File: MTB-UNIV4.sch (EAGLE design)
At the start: 122 parts, among them IC1 MEGA128-A, IC2 SN75176BP, IC3 MC7805CDTG, IC4 ULN2803A, IC5 ULN2803A, Q1 14.7456 MHz, X1A MVE252-5-V, X1B MVE252-5-V, X2A MVE252-5-V, X2B MVE252-5-V, X3 1751316, X4 1751316, X5 1751316, X6 1751316

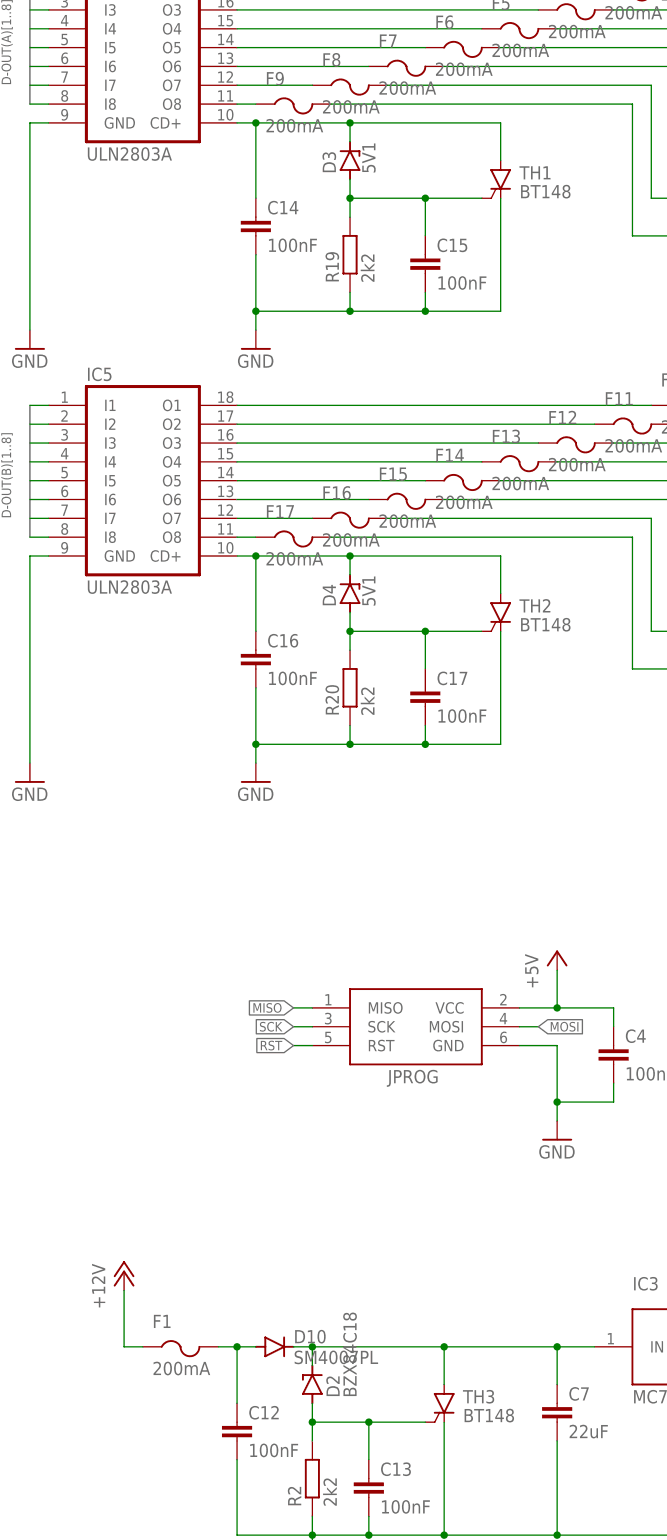
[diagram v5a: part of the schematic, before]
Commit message: Fix output Zener diodes values.
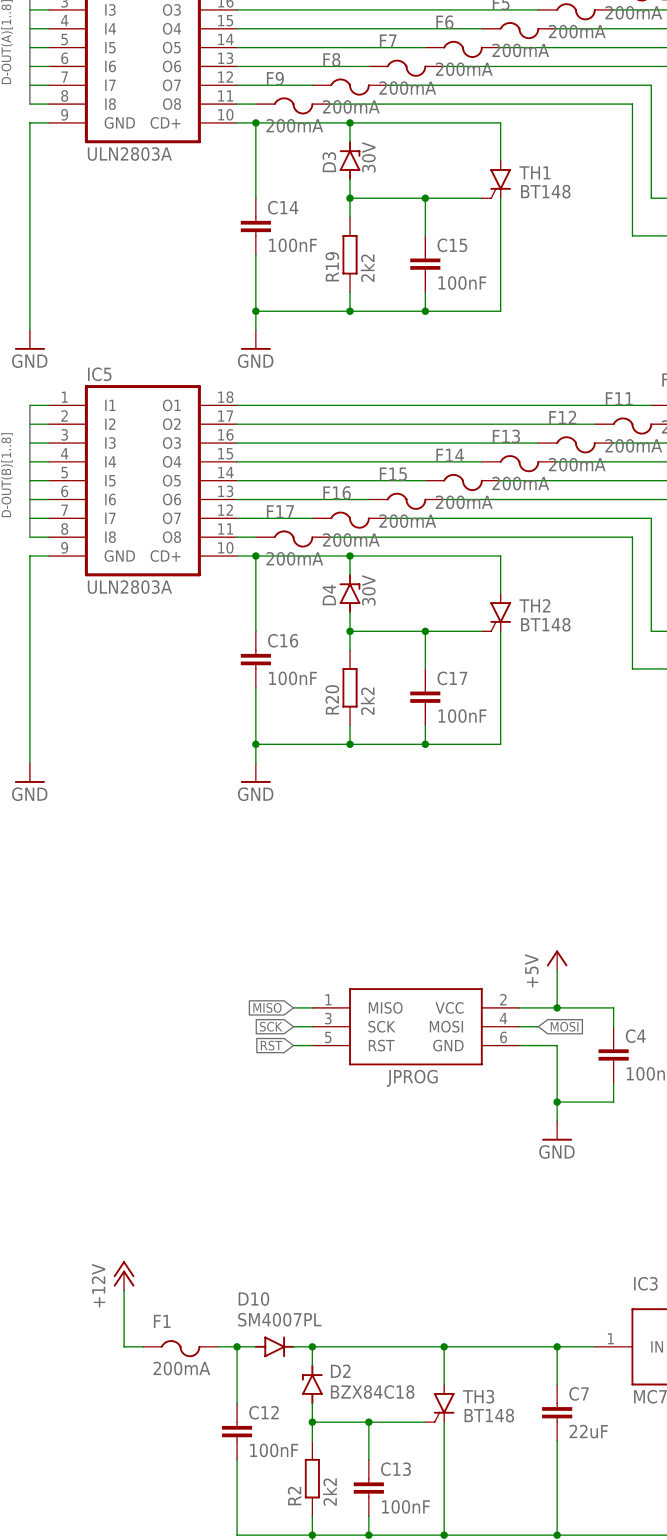
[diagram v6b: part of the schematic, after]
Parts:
- D3, D4: value 5V1 -> 30V
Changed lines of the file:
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@@
 <part name="F8" library="adafruit_edited" deviceset="PTCFUSE" device="-1206S" value="200mA"/>
 <part name="F9" library="adafruit_edited" deviceset="PTCFUSE" device="-1206S" value="200mA"/>
-<part name="D3" library="diode" library_urn="urn:adsk.eagle:library:210" deviceset="ZENER-DIODE" device="SOT23" package3d_urn="urn:adsk.eagle:package:43389/2" value="5V1"/>
-<part name="D4" library="diode" library_urn="urn:adsk.eagle:library:210" deviceset="ZENER-DIODE" device="SOT23" package3d_urn="urn:adsk.eagle:package:43389/2" value="5V1"/>
+<part name="D3" library="diode" library_urn="urn:adsk.eagle:library:210" deviceset="ZENER-DIODE" device="SOT23" package3d_urn="urn:adsk.eagle:package:43389/2" value="30V"/>
+<part name="D4" library="diode" library_urn="urn:adsk.eagle:library:210" deviceset="ZENER-DIODE" device="SOT23" package3d_urn="urn:adsk.eagle:package:43389/2" value="30V"/>
 <part name="R20" library="rcl" deviceset="R-EU_" device="R1206" value="2k2"/>
 <part name="R19" library="rcl" deviceset="R-EU_" device="R1206" value="2k2"/>
@@
 </instance>
 <instance part="D2" gate="G$1" x="292.1" y="58.42" smashed="yes" rot="MR90">
-<attribute name="NAME" x="294.005" y="56.642" size="1.778" layer="95" rot="MR90"/>
-<attribute name="VALUE" x="296.291" y="56.642" size="1.778" layer="96" rot="MR90"/>
+<attribute name="NAME" x="294.386" y="61.087" size="1.778" layer="95" rot="MR180"/>
+<attribute name="VALUE" x="294.386" y="58.293" size="1.778" layer="96" rot="MR180"/>
 </instance>
 <instance part="IC3" gate="G$1" x="342.9" y="63.5" smashed="yes">
@@
 </instance>
 <instance part="D10" gate="G$1" x="287.02" y="63.5" smashed="yes">
-<attribute name="NAME" x="289.56" y="63.9826" size="1.778" layer="95"/>
-<attribute name="VALUE" x="289.56" y="61.1886" size="1.778" layer="96"/>
+<attribute name="NAME" x="281.94" y="69.0626" size="1.778" layer="95"/>
+<attribute name="VALUE" x="281.94" y="66.2686" size="1.778" layer="96"/>
 </instance>
 </instances>

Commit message: Add LCSC numbers.
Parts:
- C1, C2: LCSC_PART (none) -> C1854
- C12, C13, C14, C15, C16, C17, C18, C19, C20, C21, C3, C4: LCSC_PART (none) -> C24497
- C7, C8: LCSC_PART (none) -> C12891
- C9, R10, R11, R12, R13, R14, R15, R16, R17, R18, R19, R2, R20, R23, R24, R3, R4, R5, R6, R7, R8: LCSC_PART (none) -> C17944
- D10: LCSC_PART (none) -> C64898
- D22, D3, D4, D5: LCSC_PART (none) -> C353849
- F1, F10, F11, F12, F13, F14, F15, F16, F17, F2, F3, F4, F5, F6, F7, F8, F9: LCSC_PART (none) -> C70067
- F18, F19, F20, F21, F22, F23, F24, F25, F27, F28, F29, F30, F31, F32, F33: LCSC_PART (none) -> C261946
- F26: LSCS_PART (none) -> C261946
- IC1: LCSC_PART (none) -> C6510
- IC3: LCSC_PART (none) -> C54285
- R1, R25: LCSC_PART (none) -> C17902

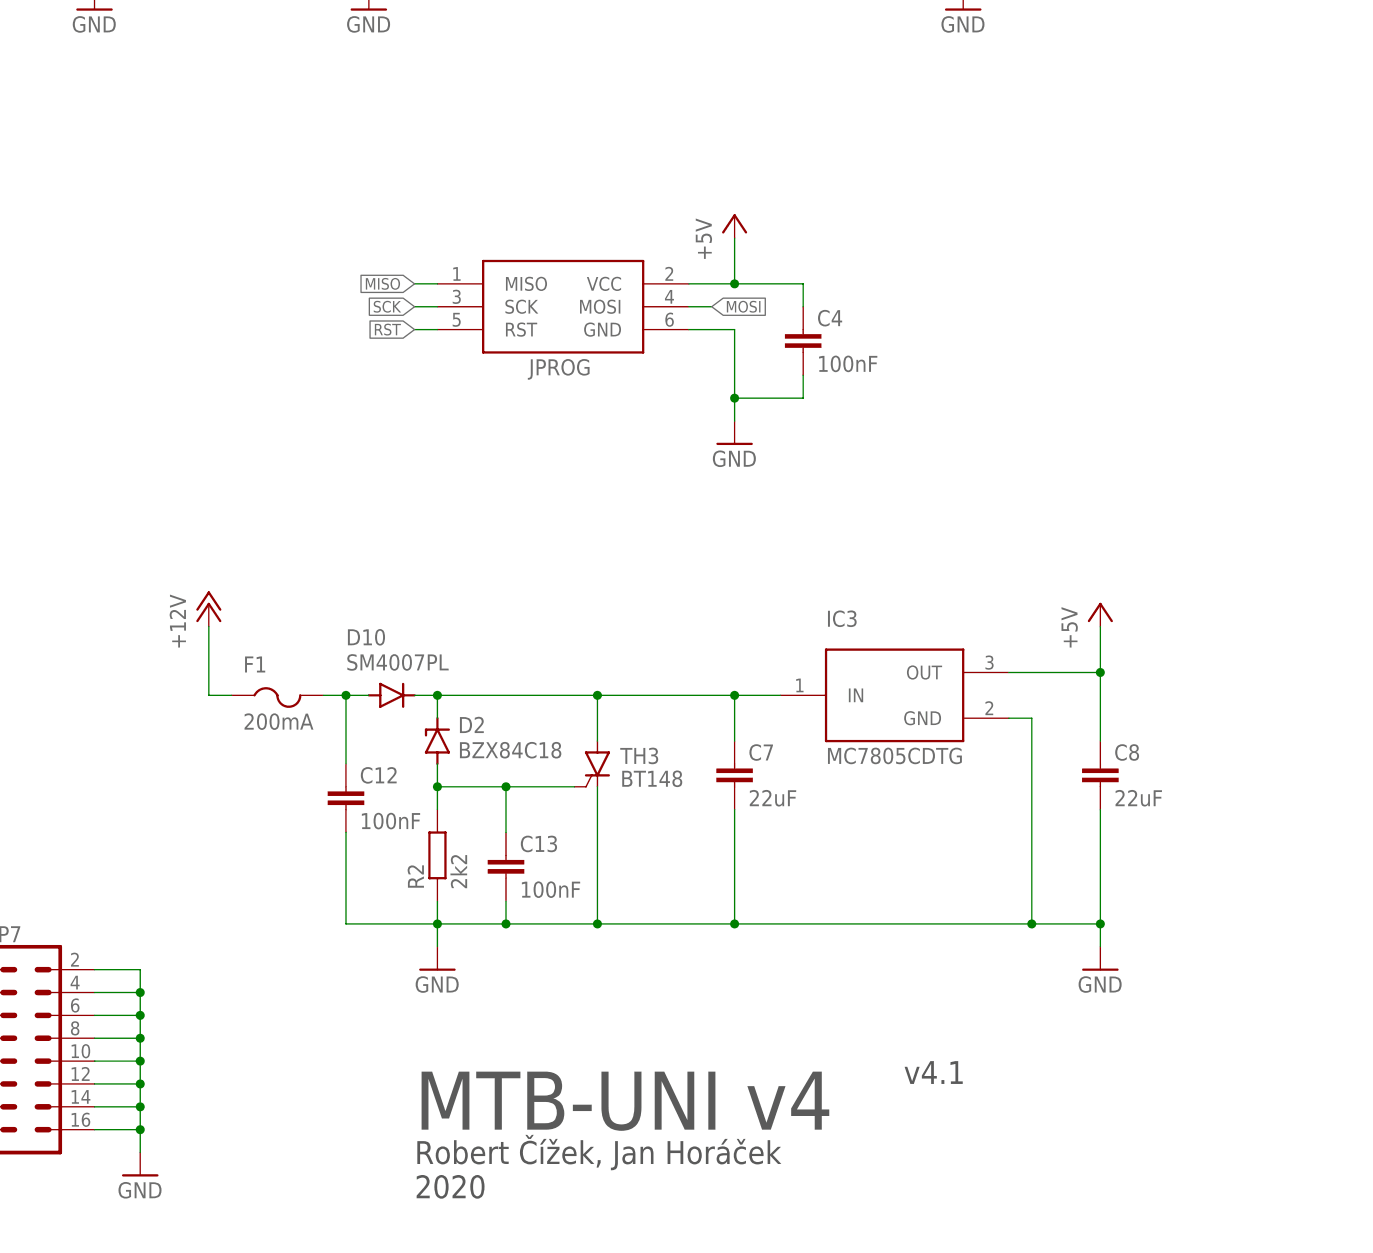
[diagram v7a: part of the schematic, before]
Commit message: Change licence to Creative Commons as this is HW.
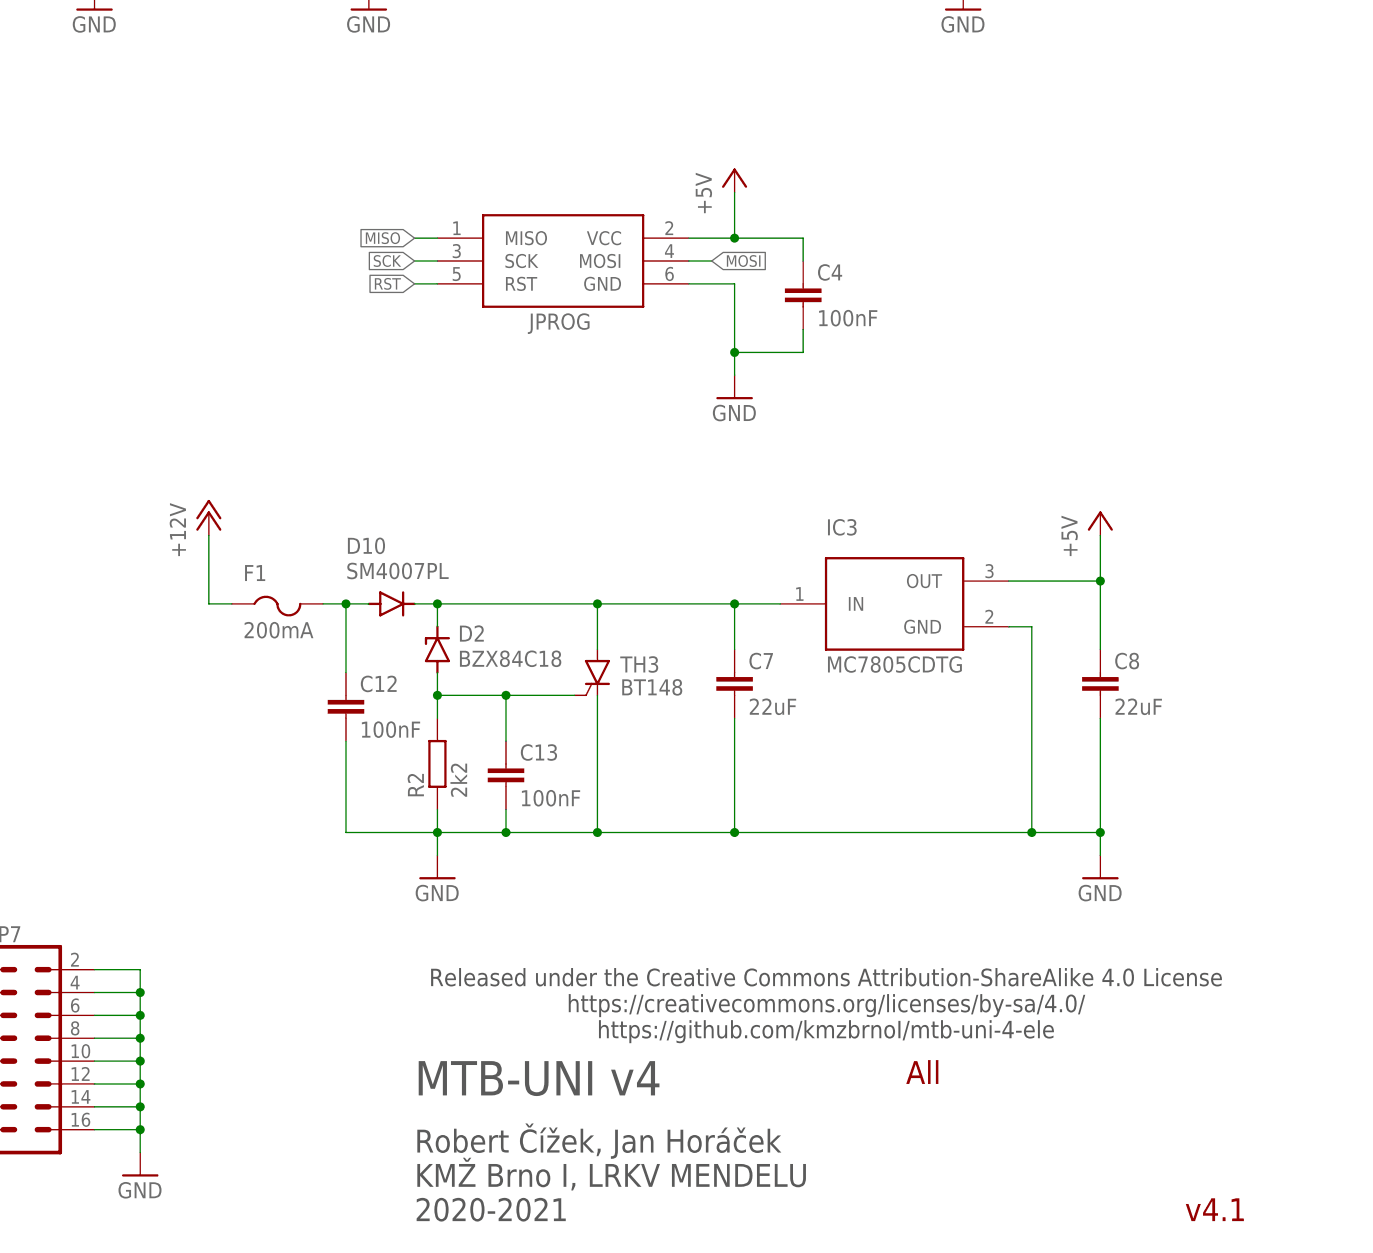
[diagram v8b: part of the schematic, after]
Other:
- note added: "All"
- note added: "Released under the Creative Commons Attribution-ShareAlike 4.0 License https://creativecommons.org/licenses/by-sa/4.0/ https://github.com/kmzbrnoI/mtb-uni-4-ele"
- note added: "Robert Čížek, Jan Horáček KMŽ Brno I, LRKV MENDELU 2020-2021"
- note removed: "Robert Čížek, Jan Horáček 2020"
- moved on the sheet: C12, C13, C4, C7, C8, D10, D2, F1, IC3, JPROG, R2, TH3
